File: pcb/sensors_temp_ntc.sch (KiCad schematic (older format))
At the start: 4 parts

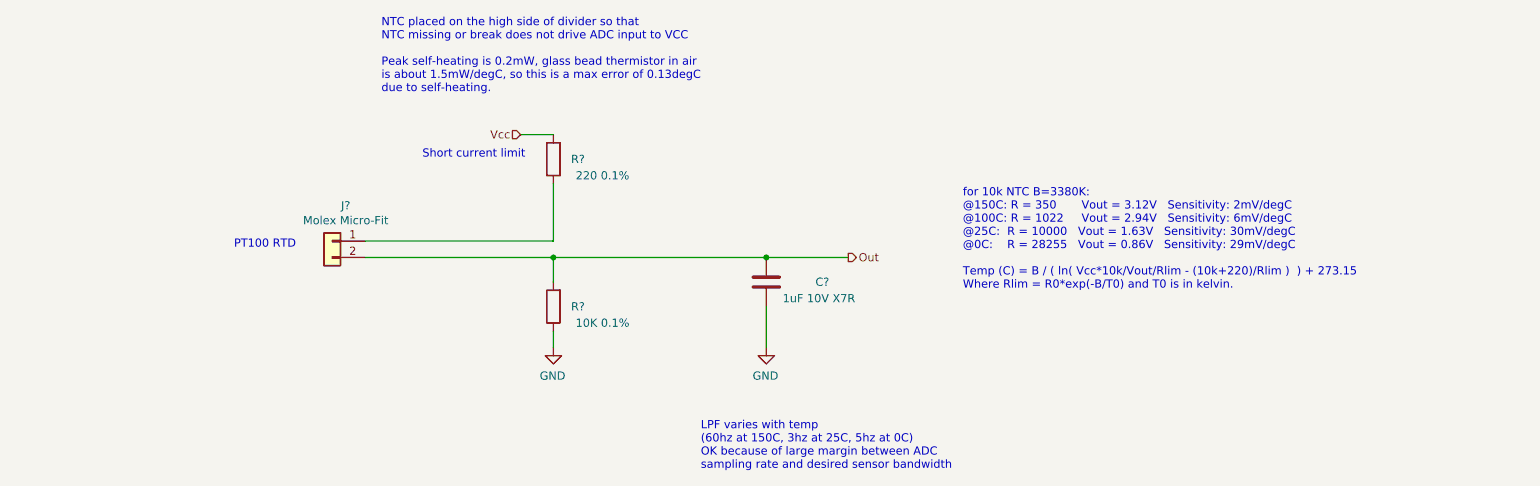
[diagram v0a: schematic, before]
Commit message: added TVS to NTC circuit
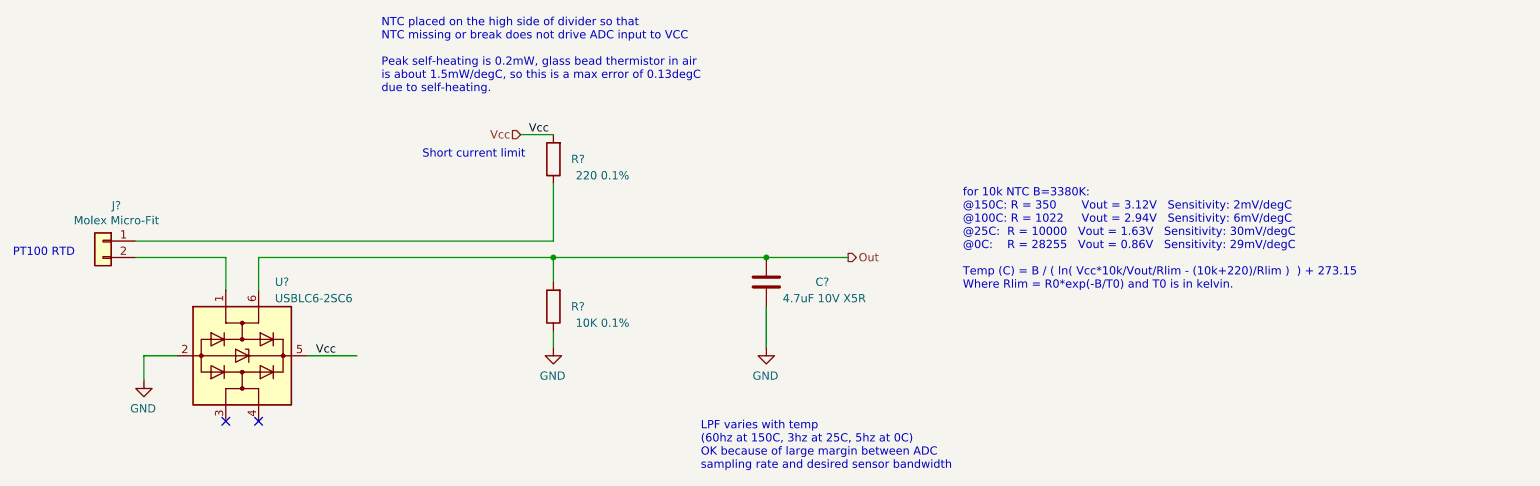
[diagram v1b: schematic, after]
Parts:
- added U?: USBLC6-2SC6, Package_TO_SOT_SMD:SOT-23-6, symbol Power_Protection:USBLC6-2SC6
- C?: value 1uF 10V X7R -> 4.7uF 10V X5R
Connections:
- wire segments 9 -> 15
- no-connect marks 0 -> 2
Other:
- moved on the sheet: J?
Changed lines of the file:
@@
 $Descr A4 11693 8268
 encoding utf-8
-Sheet 24 30
+Sheet 27 30
 Title "NTC Temperature Sensor Input"
 Date ""
@@
 L Connector_Generic:Conn_01x02 J?
 U 1 1 6010AD26
-P 2950 3200
+P 1550 3200
 AR Path="/5FCD4EEA/600F5EF3/6010AD26" Ref="J?"  Part="1"
 AR Path="/5FCD4EEA/600F7154/6010AD26" Ref="J?"  Part="1"
@@
 AR Path="/5FCD4EEA/600F71F1/6010AD26" Ref="J?"  Part="1"
 AR Path="/5FCD4EEA/600F723B/6010AD26" Ref="J?"  Part="1"
-F 0 "J?" H 2868 3417 50  0000 C CNN
-F 1 "Molex Micro-Fit" H 2868 3326 50  0000 C CNN
-F 2 "RespiraWorks_Std:Molex_Micro-Fit_3.0_43650-0215_1x02_P3.00mm_Vertical" H 2950 3200 50  0001 C CNN
-F 3 "~" H 2950 3200 50  0001 C CNN
-	1    2950 3200
+F 0 "J?" H 1468 3417 50  0000 C CNN
+F 1 "Molex Micro-Fit" H 1468 3326 50  0000 C CNN
+F 2 "RespiraWorks_Std:Molex_Micro-Fit_3.0_43650-0215_1x02_P3.00mm_Vertical" H 1550 3200 50  0001 C CNN
+F 3 "~" H 1550 3200 50  0001 C CNN
+	1    1550 3200
 	-1   0    0    -1
 $EndComp
@@
 	-1   0    0    -1
 $EndComp
-Text Notes 2350 3250 0    50   ~ 0
+Text Notes 1000 3300 0    50   ~ 0
 PT100 RTD
 $Comp
@@
 AR Path="/5FCD4EEA/600F719E/60117C61" Ref="C?"  Part="1"
 F 0 "C?" H 5900 3450 50  0000 L CNN
-F 1 "1uF 10V X7R" H 5700 3550 50  0000 L CNN
+F 1 "4.7uF 10V X5R" H 5700 3550 50  0000 L CNN
 F 2 "RespiraWorks_Std:C_0603_1608Metric" H 5638 3300 50  0001 C CNN
 F 3 "~" H 5600 3450 50  0001 C CNN
@@
 $EndComp
 Wire Wire Line
-	3150 3300 4300 3300
+	1750 3300 2300 3300
 Wire Wire Line
 	4300 3300 4300 3450
 Wire Wire Line
-	3150 3200 4300 3200
+	1750 3200 4300 3200
 Wire Wire Line
 	4300 3200 4300 2850
@@
 Wire Wire Line
 	5600 3600 5600 3850
+$Comp
+L Power_Protection:USBLC6-2SC6 U?
+U 1 1 5FFD5C58
+P 2400 3900
+F 0 "U?" V 1950 4100 50  0000 L CNN
+F 1 "USBLC6-2SC6" V 2050 4100 50  0000 L CNN
+F 2 "Package_TO_SOT_SMD:SOT-23-6" H 2400 3400 50  0001 C CNN
+F 3 "https://www.st.com/resource/en/datasheet/usblc6-2.pdf" H 2600 4250 50  0001 C CNN
+	1    2400 3900
+	0    1    1    0
+$EndComp
+Wire Wire Line
+	2500 3500 2500 3300
+Wire Wire Line
+	2500 3300 4300 3300
+Wire Wire Line
+	2300 3500 2300 3300
+NoConn ~ 2300 4300
+NoConn ~ 2500 4300
+Wire Wire Line
+	2800 3900 3100 3900
+Text Label 2850 3900 0    50   ~ 0
+Vcc
+Text Label 4150 2550 0    50   ~ 0
+Vcc
+$Comp
+L power:GND #PWR?
+U 1 1 5FFDA1EB
+P 1800 4050
+AR Path="/5FCD4B8E/5FCD4BC5/5FFDA1EB" Ref="#PWR?"  Part="1"
+AR Path="/5FCD4B8E/5FE27F70/5FFDA1EB" Ref="#PWR?"  Part="1"
+AR Path="/5FCD4B8E/5FCD4BF6/5FFDA1EB" Ref="#PWR?"  Part="1"
+AR Path="/5FCD4B8E/606EF10F/5FFDA1EB" Ref="#PWR?"  Part="1"
+AR Path="/5FCD4E9D/5FFDA1EB" Ref="#PWR?"  Part="1"
+AR Path="/5FCD4E9D/6007E2BB/5FFDA1EB" Ref="#PWR?"  Part="1"
+AR Path="/5FCD4E9D/60073FCF/5FFDA1EB" Ref="#PWR?"  Part="1"
+AR Path="/5FCD4EEA/600F5EF3/5FFDA1EB" Ref="#PWR?"  Part="1"
+AR Path="/5FCD4EEA/600F7154/5FFDA1EB" Ref="#PWR?"  Part="1"
+AR Path="/5FCD4EEA/600F719E/5FFDA1EB" Ref="#PWR?"  Part="1"
+AR Path="/5FCD4EEA/600F71F1/5FFDA1EB" Ref="#PWR?"  Part="1"
+AR Path="/5FCD4EEA/600F723B/5FFDA1EB" Ref="#PWR?"  Part="1"
+F 0 "#PWR?" H 1800 3800 50  0001 C CNN
+F 1 "GND" H 1805 3877 50  0000 C CNN
+F 2 "" H 1800 4050 50  0001 C CNN
+F 3 "" H 1800 4050 50  0001 C CNN
+	1    1800 4050
+	-1   0    0    -1
+$EndComp
+Wire Wire Line
+	2000 3900 1800 3900
+Wire Wire Line
+	1800 3900 1800 4050
 $EndSCHEMATC

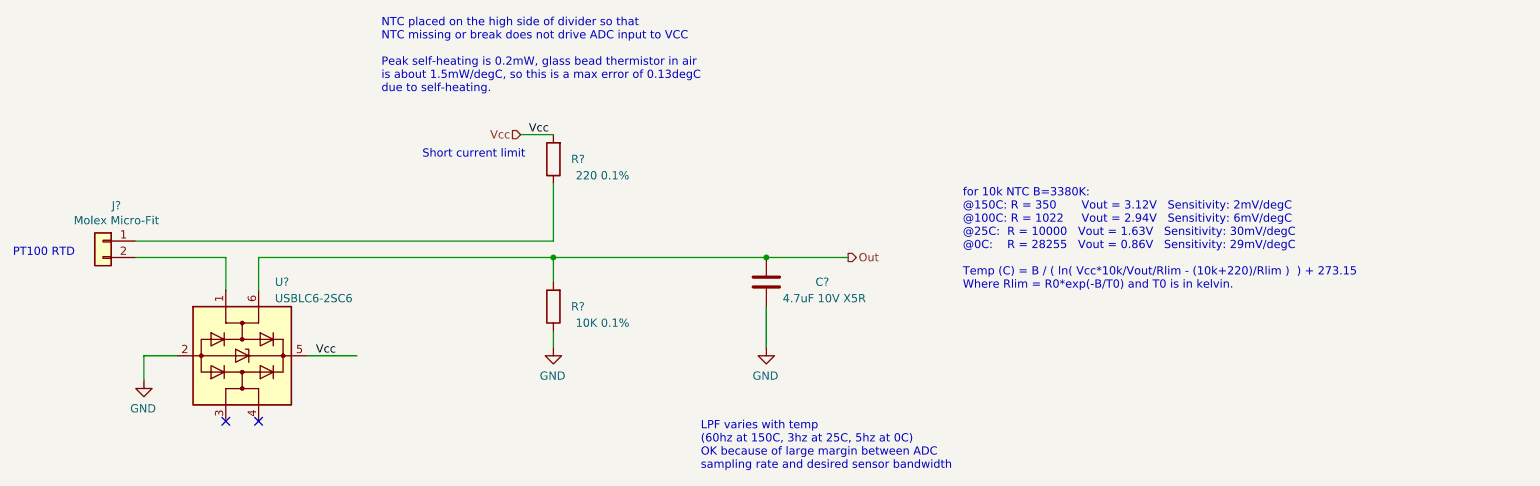
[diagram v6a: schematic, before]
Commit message: CC-I2C, BOM
Added missing pull-ups on CC-SDA, CC-SCL
First pass at BOM consolidation
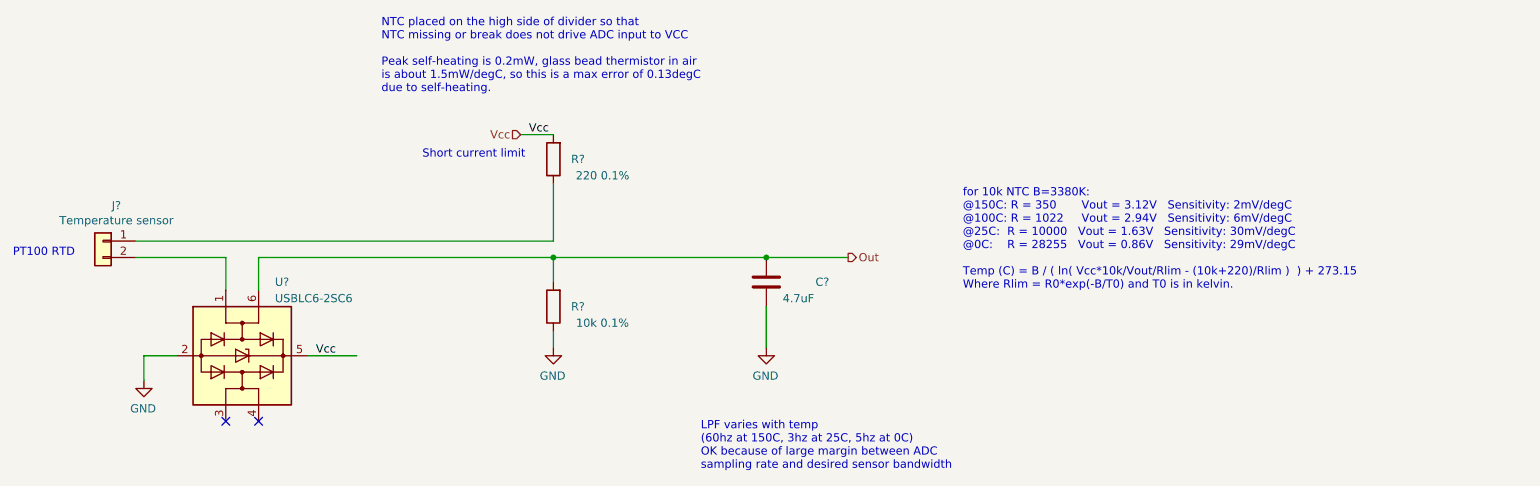
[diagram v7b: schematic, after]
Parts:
- C?: value 4.7uF 10V X5R -> 4.7uF
- J?: value Molex Micro-Fit -> Temperature sensor
- R?: value 10K 0.1% -> 10k 0.1%; Manufacturer KOA Speer -> (none)
- R?: Manufacturer KOA Speer -> (none)
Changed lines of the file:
@@
 $Descr A4 11693 8268
 encoding utf-8
-Sheet 27 38
+Sheet 22 38
 Title "NTC Temperature Sensor Input"
 Date ""
@@
 AR Path="/5FCD4EEA/600F723B/6010AD26" Ref="J?"  Part="1"
 F 0 "J?" H 1468 3417 50  0000 C CNN
-F 1 "Molex Micro-Fit" H 1468 3326 50  0000 C CNN
+F 1 "Temperature sensor" H 1468 3326 50  0000 C CNN
 F 2 "RespiraWorks_Std:Molex_Micro-Fit_3.0_43650-0215_1x02_P3.00mm_Vertical" H 1550 3200 50  0001 C CNN
 F 3 "~" H 1550 3200 50  0001 C CNN
@@
 AR Path="/5FCD4EEA/600F719E/60117C61" Ref="C?"  Part="1"
 F 0 "C?" H 5900 3450 50  0000 L CNN
-F 1 "4.7uF 10V X5R" H 5700 3550 50  0000 L CNN
+F 1 "4.7uF" H 5700 3550 50  0000 L CNN
 F 2 "RespiraWorks_Std:C_0603_1608Metric" H 5638 3300 50  0001 C CNN
 F 3 "~" H 5600 3450 50  0001 C CNN
@@
 F 2 "RespiraWorks_Std:R_0603_1608Metric" V 4230 2700 50  0001 C CNN
 F 3 "~" H 4300 2700 50  0001 C CNN
-F 4 "KOA Speer" H 4300 2700 50  0001 C CNN "Manufacturer"
+F 4 "" H 4300 2700 50  0001 C CNN "Manufacturer"
 F 5 "RK73H2BTTD1004F" H 4300 2700 50  0001 C CNN "Part Number"
 	1    4300 2700
@@
 AR Path="/5FCD4EEA/600F723B/5FFCC04E" Ref="R?"  Part="1"
 F 0 "R?" H 4150 3600 50  0000 C CNN
-F 1 "10K 0.1%" H 4000 3700 50  0000 C CNN
+F 1 "10k 0.1%" H 4000 3700 50  0000 C CNN
 F 2 "RespiraWorks_Std:R_0603_1608Metric" V 4230 3600 50  0001 C CNN
 F 3 "~" H 4300 3600 50  0001 C CNN
-F 4 "KOA Speer" H 4300 3600 50  0001 C CNN "Manufacturer"
+F 4 "" H 4300 3600 50  0001 C CNN "Manufacturer"
 F 5 "RK73H2BTTD1004F" H 4300 3600 50  0001 C CNN "Part Number"
 	1    4300 3600

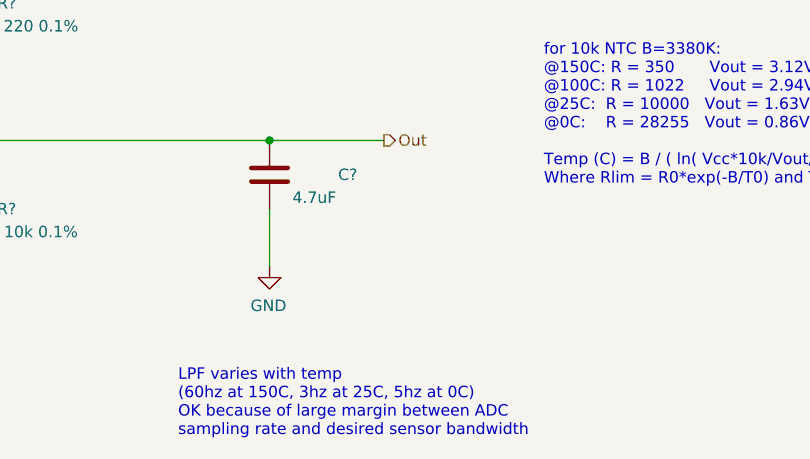
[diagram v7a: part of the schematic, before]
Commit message: BOM
More BOM consolidation with bulk capacitors + changed tantalum stepper caps to aluminum, added bulk cap to PSol driver
Made stepper's 3.3V power naming consistent with others (3.3V->3V3)
Slightly increased current limit on PSOL/heater driver
Changed 3906 transistors to 2907 to better support +5V_Batt current
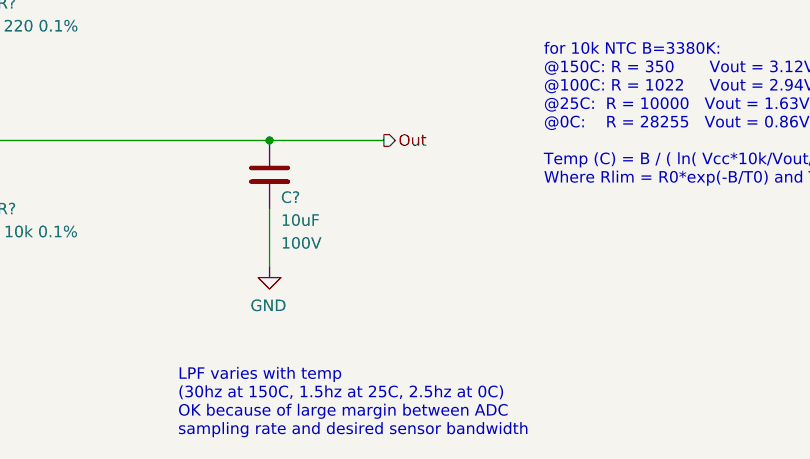
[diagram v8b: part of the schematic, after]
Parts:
- removed C?: 4.7uF, RespiraWorks_Std:C_0603_1608Metric, symbol Device:C
- added C?: 10uF, RespiraWorks_Std:C_1210_3225Metric, symbol Device:C
- R? (x2): Part Number RK73H2BTTD1004F -> (none)
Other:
- note added: "LPF varies with temp\n(30hz at 150C, 1.5hz at 25C, 2.5hz at 0C)\nOK because of large margin between ADC \nsampling rate and desired sensor bandwidth"
- note removed: "LPF varies with temp\n(60hz at 150C, 3hz at 25C, 5hz at 0C)\nOK because of large margin between ADC \nsampling rate and desired sensor bandwidth"
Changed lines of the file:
@@
 $Descr A4 11693 8268
 encoding utf-8
-Sheet 22 38
+Sheet 25 38
 Title "NTC Temperature Sensor Input"
 Date ""
@@
 Text Notes 1000 3300 0    50   ~ 0
 PT100 RTD
-$Comp
-L Device:C C?
-U 1 1 60117C61
-P 5600 3450
-AR Path="/5FCD4B8E/5FCD4BC5/60117C61" Ref="C?"  Part="1"
-AR Path="/5FCD4B8E/5FE27F70/60117C61" Ref="C?"  Part="1"
-AR Path="/5FCD4B8E/5FCD4BF6/60117C61" Ref="C?"  Part="1"
-AR Path="/5FCD4B8E/606EF10F/60117C61" Ref="C?"  Part="1"
-AR Path="/5FCD4E9D/60117C61" Ref="C?"  Part="1"
-AR Path="/5FCD4E9D/6007E2BB/60117C61" Ref="C?"  Part="1"
-AR Path="/5FCD4E9D/60073FCF/60117C61" Ref="C?"  Part="1"
-AR Path="/5FCD4E9D/600630A6/60117C61" Ref="C?"  Part="1"
-AR Path="/5FCD4E9D/6007AC3B/60117C61" Ref="C?"  Part="1"
-AR Path="/5FCD4E9D/6007DA64/60117C61" Ref="C?"  Part="1"
-AR Path="/5FCD4E9D/6007BD34/60117C61" Ref="C?"  Part="1"
-AR Path="/5FCD4EEA/600F5EF3/60117C61" Ref="C?"  Part="1"
-AR Path="/5FCD4EEA/600F71F1/60117C61" Ref="C?"  Part="1"
-AR Path="/5FCD4EEA/600F723B/60117C61" Ref="C?"  Part="1"
-AR Path="/5FCD4EEA/600F7154/60117C61" Ref="C?"  Part="1"
-AR Path="/5FCD4EEA/600F719E/60117C61" Ref="C?"  Part="1"
-F 0 "C?" H 5900 3450 50  0000 L CNN
-F 1 "4.7uF" H 5700 3550 50  0000 L CNN
-F 2 "RespiraWorks_Std:C_0603_1608Metric" H 5638 3300 50  0001 C CNN
-F 3 "~" H 5600 3450 50  0001 C CNN
-	1    5600 3450
-	1    0    0    1
-$EndComp
 $Comp
 L power:GND #PWR?
@@
 	-1   0    0    -1
 $EndComp
-Wire Wire Line
-	5600 3300 6100 3300
 Text Notes 5200 4600 0    50   ~ 0
-LPF varies with temp\n(60hz at 150C, 3hz at 25C, 5hz at 0C)\nOK because of large margin between ADC \nsampling rate and desired sensor bandwidth
-Connection ~ 5600 3300
+LPF varies with temp\n(30hz at 150C, 1.5hz at 25C, 2.5hz at 0C)\nOK because of large margin between ADC \nsampling rate and desired sensor bandwidth
 Text Notes 6800 3500 0    50   ~ 0
 for 10k NTC B=3380K:\n@150C: R = 350       Vout = 3.12V   Sensitivity: 2mV/degC\n@100C: R = 1022     Vout = 2.94V   Sensitivity: 6mV/degC\n@25C:  R = 10000   Vout = 1.63V   Sensitivity: 30mV/degC\n@0C:    R = 28255   Vout = 0.86V   Sensitivity: 29mV/degC\n\nTemp (C) = B / ( ln( Vcc*10k/Vout/Rlim - (10k+220)/Rlim )  ) + 273.15\nWhere Rlim = R0*exp(-B/T0) and T0 is in kelvin.
@@
 F 3 "~" H 4300 2700 50  0001 C CNN
 F 4 "" H 4300 2700 50  0001 C CNN "Manufacturer"
-F 5 "RK73H2BTTD1004F" H 4300 2700 50  0001 C CNN "Part Number"
 	1    4300 2700
 	-1   0    0    1
@@
 F 3 "~" H 4300 3600 50  0001 C CNN
 F 4 "" H 4300 3600 50  0001 C CNN "Manufacturer"
-F 5 "RK73H2BTTD1004F" H 4300 3600 50  0001 C CNN "Part Number"
 	1    4300 3600
 	-1   0    0    1
@@
 Wire Wire Line
 	4300 3750 4300 3850
-Wire Wire Line
-	4300 3300 5600 3300
 Connection ~ 4300 3300
 Wire Wire Line
@@
 Wire Wire Line
 	1800 3900 1800 4050
+$Comp
+L Device:C C?
+U 1 1 6071F4E4
+P 5600 3450
+AR Path="/601A64F8/6071F4E4" Ref="C?"  Part="1"
+AR Path="/601A64F8/60567144/6071F4E4" Ref="C?"  Part="1"
+AR Path="/6023BF6A/60567144/6071F4E4" Ref="C?"  Part="1"
+AR Path="/5FCD4B8E/603C510C/60567144/6071F4E4" Ref="C?"  Part="1"
+AR Path="/6041384A/60567144/6071F4E4" Ref="C?"  Part="1"
+AR Path="/5FCD4EEA/600F71F1/6071F4E4" Ref="C?"  Part="1"
+AR Path="/5FCD4EEA/600F5EF3/6071F4E4" Ref="C?"  Part="1"
+AR Path="/5FCD4EEA/600F7154/6071F4E4" Ref="C?"  Part="1"
+AR Path="/5FCD4EEA/600F719E/6071F4E4" Ref="C?"  Part="1"
+AR Path="/5FCD4EEA/600F723B/6071F4E4" Ref="C?"  Part="1"
+F 0 "C?" H 5650 3350 50  0000 L CNN
+F 1 "10uF" H 5650 3250 50  0000 L CNN
+F 2 "RespiraWorks_Std:C_1210_3225Metric" H 5638 3300 50  0001 C CNN
+F 3 "~" H 5600 3450 50  0001 C CNN
+F 4 "100V" H 5650 3150 50  0000 L CNN "Voltage"
+F 5 "X7S" H 5600 3450 50  0001 C CNN "Dielectric"
+F 6 "Murata" H 5600 3450 50  0001 C CNN "Manufacturer"
+F 7 "GRM32EC72A106KE05L" H 5600 3450 50  0001 C CNN "Manufacturer PN"
+	1    5600 3450
+	1    0    0    -1
+$EndComp
+Wire Wire Line
+	4300 3300 5600 3300
+Connection ~ 5600 3300
+Wire Wire Line
+	5600 3300 6100 3300
 $EndSCHEMATC
